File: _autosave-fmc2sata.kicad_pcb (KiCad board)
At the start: 2 copper layers, 51 x 61 mm, 32 parts, among them J1 ASP-134488-01, J2 1-2199230-6, J3 10034814-001LF, U1 TPS565208, U2 TPS565208

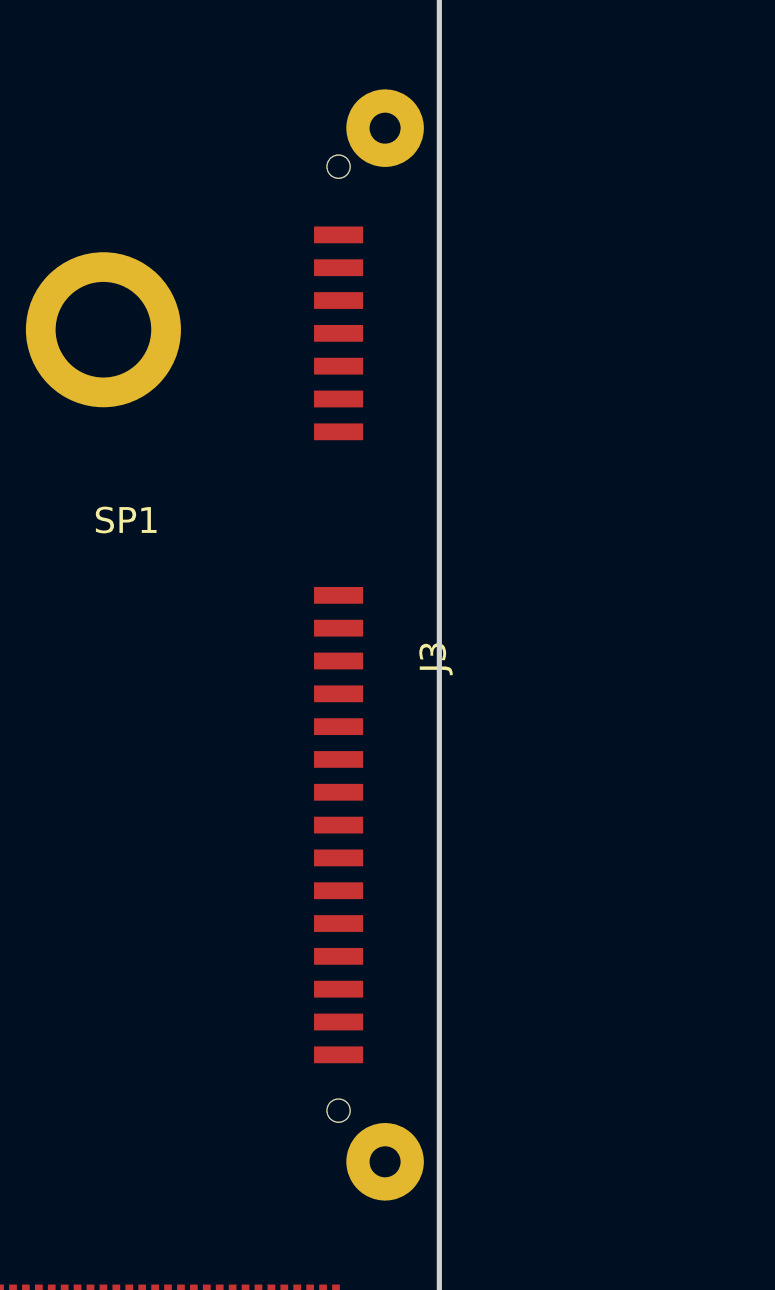
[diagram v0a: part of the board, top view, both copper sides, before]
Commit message: Add 2.5" SATA connector and 150MHz LVDS REF CLK generator
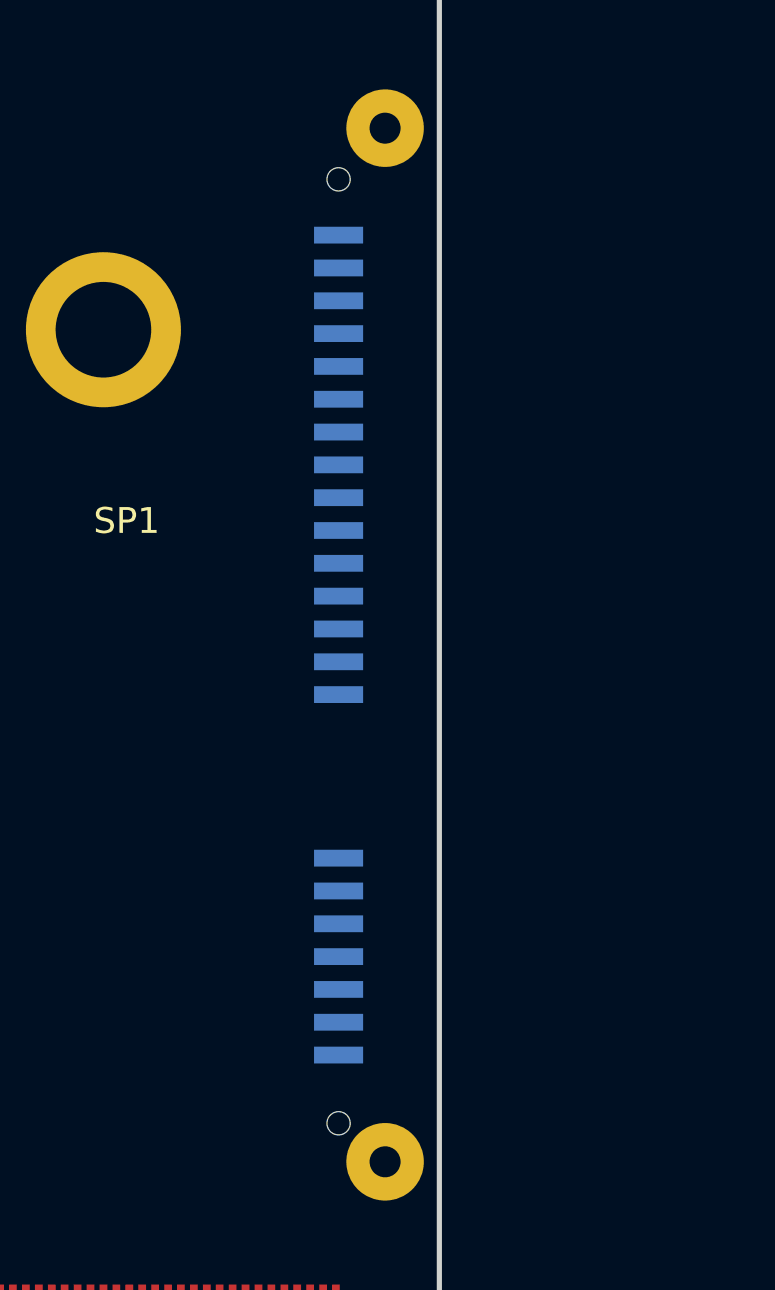
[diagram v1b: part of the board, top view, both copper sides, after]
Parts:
- J3: moved to B.Cu
- turned J3 to 270 degrees
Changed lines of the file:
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@@
     (add_net SATA_FLAG)
   )
-  (module antmicro-footprints:10034814-001LF (layer F.Cu)
-    (at 120.9 72.2 90)
-    (fp_text reference J3 (at -0.46 1.88 90) (layer F.SilkS)
+  (module antmicro-footprints:10034814-001LF (layer B.Cu)
+    (at 120.9 72.2 270)
+    (fp_text reference J3 (at -0.46 -1.88 270) (layer B.SilkS)
+      (effects (font (size 1 1) (thickness 0.15)) (justify mirror))
+    )
+    (fp_text value 10034814-001LF (at 0 0.5 270) (layer F.Fab)
       (effects (font (size 1 1) (thickness 0.15)))
     )
-    (fp_text value 10034814-001LF (at 0 -0.5 90) (layer F.Fab)
-      (effects (font (size 1 1) (thickness 0.15)))
-    )
-    (pad 15B smd rect (at -15.86 -1.8 90) (size 0.65 1.9) (layers F.Cu F.Paste F.Mask)
+    (pad 15B smd rect (at -15.86 1.8 270) (size 0.65 1.9) (layers B.Cu B.Paste B.Mask)
       (net 154 "Net-(J3-Pad13B)"))
-    (pad 14B smd rect (at -14.59 -1.8 90) (size 0.65 1.9) (layers F.Cu F.Paste F.Mask)
+    (pad 14B smd rect (at -14.59 1.8 270) (size 0.65 1.9) (layers B.Cu B.Paste B.Mask)
       (net 154 "Net-(J3-Pad13B)"))
-    (pad 13B smd rect (at -13.32 -1.8 90) (size 0.65 1.9) (layers F.Cu F.Paste F.Mask)
+    (pad 13B smd rect (at -13.32 1.8 270) (size 0.65 1.9) (layers B.Cu B.Paste B.Mask)
       (net 154 "Net-(J3-Pad13B)"))
-    (pad 12B smd rect (at -12.05 -1.8 90) (size 0.65 1.9) (layers F.Cu F.Paste F.Mask)
+    (pad 12B smd rect (at -12.05 1.8 270) (size 0.65 1.9) (layers B.Cu B.Paste B.Mask)
       (net 2 GND))
-    (pad 11B smd rect (at -10.78 -1.8 90) (size 0.65 1.9) (layers F.Cu F.Paste F.Mask)
+    (pad 11B smd rect (at -10.78 1.8 270) (size 0.65 1.9) (layers B.Cu B.Paste B.Mask)
       (net 155 "Net-(J3-Pad11B)"))
-    (pad 10B smd rect (at -9.51 -1.8 90) (size 0.65 1.9) (layers F.Cu F.Paste F.Mask)
+    (pad 10B smd rect (at -9.51 1.8 270) (size 0.65 1.9) (layers B.Cu B.Paste B.Mask)
       (net 2 GND))
-    (pad 9B smd rect (at -8.24 -1.8 90) (size 0.65 1.9) (layers F.Cu F.Paste F.Mask)
+    (pad 9B smd rect (at -8.24 1.8 270) (size 0.65 1.9) (layers B.Cu B.Paste B.Mask)
       (net 156 "Net-(J3-Pad7B)"))
-    (pad 8B smd rect (at -6.97 -1.8 90) (size 0.65 1.9) (layers F.Cu F.Paste F.Mask)
+    (pad 8B smd rect (at -6.97 1.8 270) (size 0.65 1.9) (layers B.Cu B.Paste B.Mask)
       (net 156 "Net-(J3-Pad7B)"))
-    (pad 7B smd rect (at -5.7 -1.8 90) (size 0.65 1.9) (layers F.Cu F.Paste F.Mask)
+    (pad 7B smd rect (at -5.7 1.8 270) (size 0.65 1.9) (layers B.Cu B.Paste B.Mask)
       (net 156 "Net-(J3-Pad7B)"))
-    (pad 6B smd rect (at -4.43 -1.8 90) (size 0.65 1.9) (layers F.Cu F.Paste F.Mask)
+    (pad 6B smd rect (at -4.43 1.8 270) (size 0.65 1.9) (layers B.Cu B.Paste B.Mask)
       (net 2 GND))
-    (pad 5B smd rect (at -3.16 -1.8 90) (size 0.65 1.9) (layers F.Cu F.Paste F.Mask)
+    (pad 5B smd rect (at -3.16 1.8 270) (size 0.65 1.9) (layers B.Cu B.Paste B.Mask)
       (net 2 GND))
-    (pad 4B smd rect (at -1.89 -1.8 90) (size 0.65 1.9) (layers F.Cu F.Paste F.Mask)
+    (pad 4B smd rect (at -1.89 1.8 270) (size 0.65 1.9) (layers B.Cu B.Paste B.Mask)
       (net 2 GND))
-    (pad 3B smd rect (at -0.62 -1.8 90) (size 0.65 1.9) (layers F.Cu F.Paste F.Mask)
+    (pad 3B smd rect (at -0.62 1.8 270) (size 0.65 1.9) (layers B.Cu B.Paste B.Mask)
       (net 157 "Net-(J3-Pad1B)"))
-    (pad 2B smd rect (at 0.65 -1.8 90) (size 0.65 1.9) (layers F.Cu F.Paste F.Mask)
+    (pad 2B smd rect (at 0.65 1.8 270) (size 0.65 1.9) (layers B.Cu B.Paste B.Mask)
       (net 157 "Net-(J3-Pad1B)"))
-    (pad 7A smd rect (at 8.25 -1.8 90) (size 0.65 1.9) (layers F.Cu F.Paste F.Mask)
+    (pad 7A smd rect (at 8.25 1.8 270) (size 0.65 1.9) (layers B.Cu B.Paste B.Mask)
       (net 2 GND))
-    (pad 6A smd rect (at 9.52 -1.8 90) (size 0.65 1.9) (layers F.Cu F.Paste F.Mask)
+    (pad 6A smd rect (at 9.52 1.8 270) (size 0.65 1.9) (layers B.Cu B.Paste B.Mask)
       (net 158 "Net-(J3-Pad6A)"))
-    (pad 5A smd rect (at 10.79 -1.8 90) (size 0.65 1.9) (layers F.Cu F.Paste F.Mask)
+    (pad 5A smd rect (at 10.79 1.8 270) (size 0.65 1.9) (layers B.Cu B.Paste B.Mask)
       (net 159 "Net-(J3-Pad5A)"))
-    (pad 4A smd rect (at 12.06 -1.8 90) (size 0.65 1.9) (layers F.Cu F.Paste F.Mask)
+    (pad 4A smd rect (at 12.06 1.8 270) (size 0.65 1.9) (layers B.Cu B.Paste B.Mask)
       (net 2 GND))
-    (pad 3A smd rect (at 13.33 -1.8 90) (size 0.65 1.9) (layers F.Cu F.Paste F.Mask)
+    (pad 3A smd rect (at 13.33 1.8 270) (size 0.65 1.9) (layers B.Cu B.Paste B.Mask)
       (net 160 "Net-(J3-Pad3A)"))
-    (pad 2A smd rect (at 14.6 -1.8 90) (size 0.65 1.9) (layers F.Cu F.Paste F.Mask)
+    (pad 2A smd rect (at 14.6 1.8 270) (size 0.65 1.9) (layers B.Cu B.Paste B.Mask)
       (net 161 "Net-(J3-Pad2A)"))
-    (pad 1A smd rect (at 15.87 -1.8 90) (size 0.65 1.9) (layers F.Cu F.Paste F.Mask)
+    (pad 1A smd rect (at 15.87 1.8 270) (size 0.65 1.9) (layers B.Cu B.Paste B.Mask)
       (net 2 GND))
-    (pad 1B smd rect (at 1.92 -1.8 90) (size 0.65 1.9) (layers F.Cu F.Paste F.Mask)
+    (pad 1B smd rect (at 1.92 1.8 270) (size 0.65 1.9) (layers B.Cu B.Paste B.Mask)
       (net 157 "Net-(J3-Pad1B)"))
-    (pad "" np_thru_hole circle (at 18.51 -1.8 90) (size 0.9 0.9) (drill 0.9) (layers *.Cu *.Mask))
-    (pad "" np_thru_hole circle (at -18.02 -1.8 90) (size 0.9 0.9) (drill 0.9) (layers *.Cu *.Mask))
-    (pad "" thru_hole circle (at -20 0 90) (size 3 3) (drill 1.2) (layers *.Cu *.Mask))
-    (pad "" thru_hole circle (at 20 0 90) (size 3 3) (drill 1.2) (layers *.Cu *.Mask))
+    (pad "" np_thru_hole circle (at 18.51 1.8 270) (size 0.9 0.9) (drill 0.9) (layers *.Cu *.Mask))
+    (pad "" np_thru_hole circle (at -18.02 1.8 270) (size 0.9 0.9) (drill 0.9) (layers *.Cu *.Mask))
+    (pad "" thru_hole circle (at -20 0 270) (size 3 3) (drill 1.2) (layers *.Cu *.Mask))
+    (pad "" thru_hole circle (at 20 0 270) (size 3 3) (drill 1.2) (layers *.Cu *.Mask))
     (model ${ANT3DMDL}/10034814001.stp
       (offset (xyz 0 -2.1 3.8))
